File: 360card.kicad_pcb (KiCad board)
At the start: 2 copper layers, 23 parts

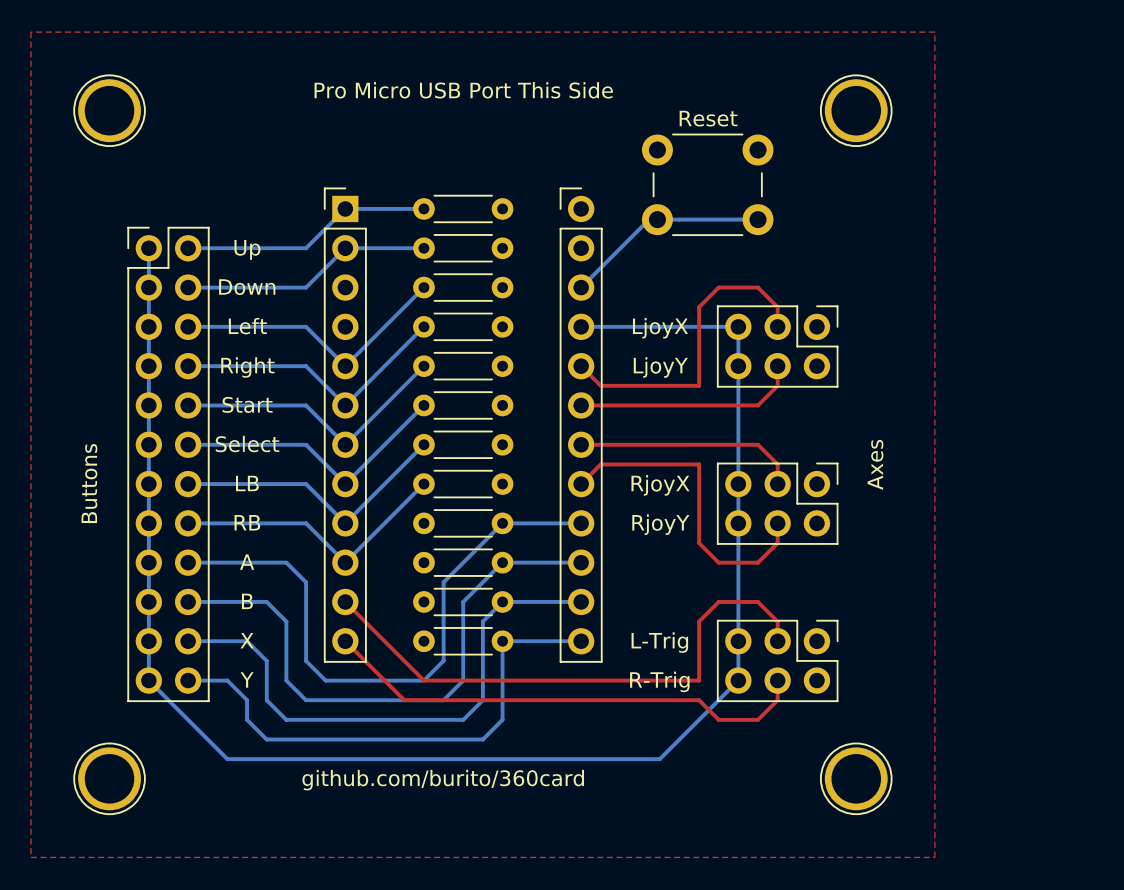
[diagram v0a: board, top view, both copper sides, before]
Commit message: Reworked the PCB design
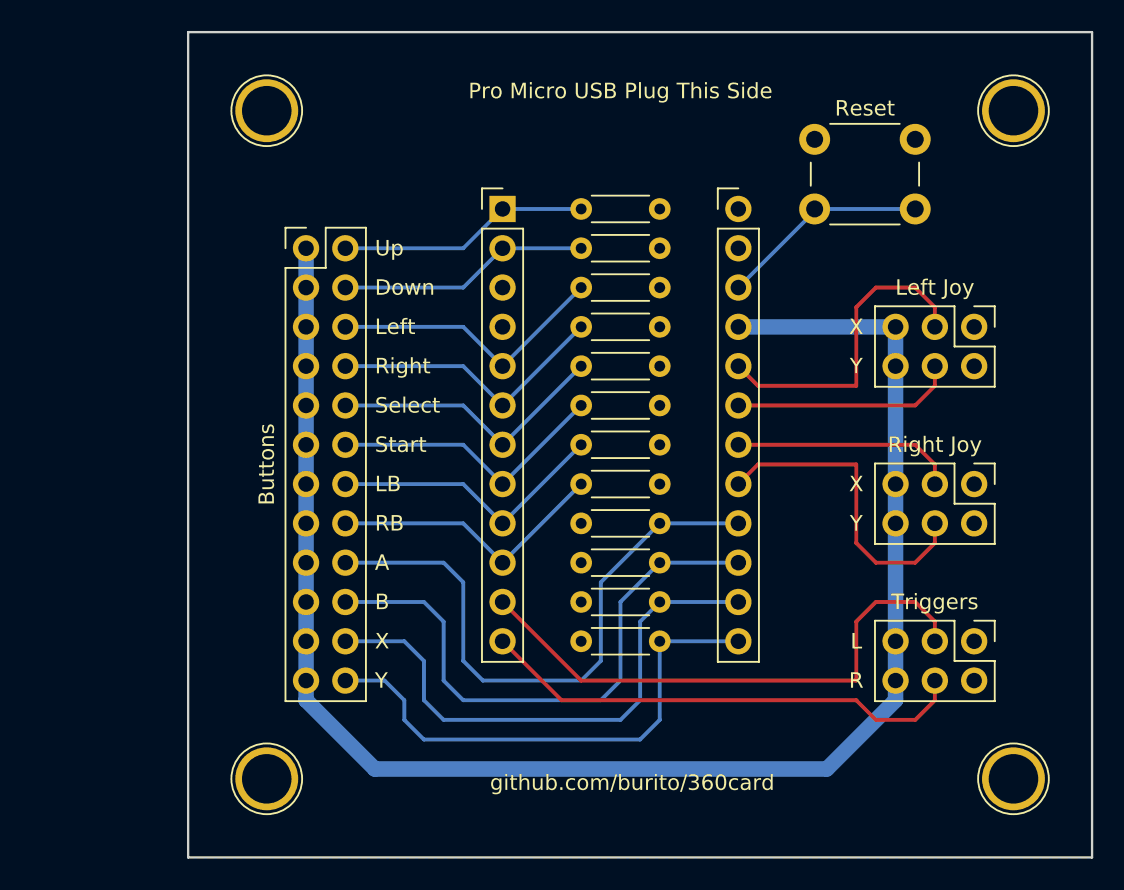
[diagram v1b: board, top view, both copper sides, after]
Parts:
- removed A, B, Down, LB, Left, RB, Right, Select, Start, Up, X, Y: R, Resistors_THT:R_Axial_DIN0204_L3.6mm_D1.6mm_P5.08mm_Horizontal
- removed Axes, LjoyY, R-Trig, RjoyY: 1pin, Connectors:1pin
- removed L-Trig, LjoyX, RjoyX: CONN_02X03, Pin_Headers:Pin_Header_Straight_2x03_Pitch2.54mm
- removed Pro Micro USB Port This Side: CONN_01X12, Socket_Strips:Socket_Strip_Straight_1x12_Pitch2.54mm
- removed github.com/burito/360card: CONN_01X12, Socket_Strips:Socket_Strip_Straight_1x12_Pitch2.54mm
- added J2: Conn_01x12_Female, Socket_Strips:Socket_Strip_Straight_1x12_Pitch2.54mm, F.Cu at (149.9, 105.4)
- added J3: Conn_01x12_Female, Socket_Strips:Socket_Strip_Straight_1x12_Pitch2.54mm, F.Cu at (165.1, 105.4)
- added Left Joy: Left Joystick, Pin_Headers:Pin_Header_Straight_2x03_Pitch2.54mm, F.Cu at (180.3, 113.0)
- added R1: 10k, Resistors_THT:R_Axial_DIN0204_L3.6mm_D1.6mm_P5.08mm_Horizontal, F.Cu at (160.0, 105.4)
- added R10: 10k, Resistors_THT:R_Axial_DIN0204_L3.6mm_D1.6mm_P5.08mm_Horizontal, F.Cu at (160.0, 128.3)
- added R11: 10k, Resistors_THT:R_Axial_DIN0204_L3.6mm_D1.6mm_P5.08mm_Horizontal, F.Cu at (160.0, 130.8)
- added R12: 10k, Resistors_THT:R_Axial_DIN0204_L3.6mm_D1.6mm_P5.08mm_Horizontal, F.Cu at (160.0, 133.3)
- added R2: 10k, Resistors_THT:R_Axial_DIN0204_L3.6mm_D1.6mm_P5.08mm_Horizontal, F.Cu at (160.0, 108.0)
- added R3: 10k, Resistors_THT:R_Axial_DIN0204_L3.6mm_D1.6mm_P5.08mm_Horizontal, F.Cu at (160.0, 110.5)
- added R4: 10k, Resistors_THT:R_Axial_DIN0204_L3.6mm_D1.6mm_P5.08mm_Horizontal, F.Cu at (160.0, 113.0)
- added R5: 10k, Resistors_THT:R_Axial_DIN0204_L3.6mm_D1.6mm_P5.08mm_Horizontal, F.Cu at (160.0, 115.6)
- added R6: 10k, Resistors_THT:R_Axial_DIN0204_L3.6mm_D1.6mm_P5.08mm_Horizontal, F.Cu at (160.0, 118.1)
- added R7: 10k, Resistors_THT:R_Axial_DIN0204_L3.6mm_D1.6mm_P5.08mm_Horizontal, F.Cu at (160.0, 120.7)
- added R8: 10k, Resistors_THT:R_Axial_DIN0204_L3.6mm_D1.6mm_P5.08mm_Horizontal, F.Cu at (160.0, 123.2)
- added R9: 10k, Resistors_THT:R_Axial_DIN0204_L3.6mm_D1.6mm_P5.08mm_Horizontal, F.Cu at (160.0, 125.7)
- added REF**: 1pin, Connectors:1pin, F.Cu at (134.6, 99.1)
- added REF**: 1pin, Connectors:1pin, F.Cu at (182.9, 99.1)
- added REF**: 1pin, Connectors:1pin, F.Cu at (182.9, 142.2)
- added REF**: 1pin, Connectors:1pin, F.Cu at (134.6, 142.2)
- added Right Joy: Right Joystick, Pin_Headers:Pin_Header_Straight_2x03_Pitch2.54mm, F.Cu at (180.3, 123.2)
- added Triggers: Triggers, Pin_Headers:Pin_Header_Straight_2x03_Pitch2.54mm, F.Cu at (180.3, 133.3)
- Buttons: value CONN_02X12 -> Buttons
- Reset: value SW_Push -> Reset
- moved Reset 10.2 mm to (170.0, 100.9)
- moved Buttons 10.2 mm to (137.2, 108.0)
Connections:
- net /5V renamed /+5V
- Reset pad 1: /Ground -> /GND
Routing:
- net /+5V: track 103.3 -> 105.3 mm
- added copper zone on F.Cu, net /GND
- removed copper zone on F.Cu, net /Ground
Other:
- board outline added: 58.4 x 53.3 mm
- net class +5V added: clearance 0.75, trace_width 1, via_dia 0.6, via_drill 0.4
- board text added: "A"
- board text added: "B"
- board text added: "Down"
- board text added: "L"
- board text added: "LB"
- board text added: "Left"
- board text added: "Pro Micro USB Plug This Side"
- board text added: "R"
- board text added: "RB"
- board text added: "Right"
- board text added: "Select"
- board text added: "Start"
- board text added: "Up"
- board text added: "X"
- board text added: "Y"
- board text added: "github.com/burito/360card"
